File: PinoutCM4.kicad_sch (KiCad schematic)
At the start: 1 part

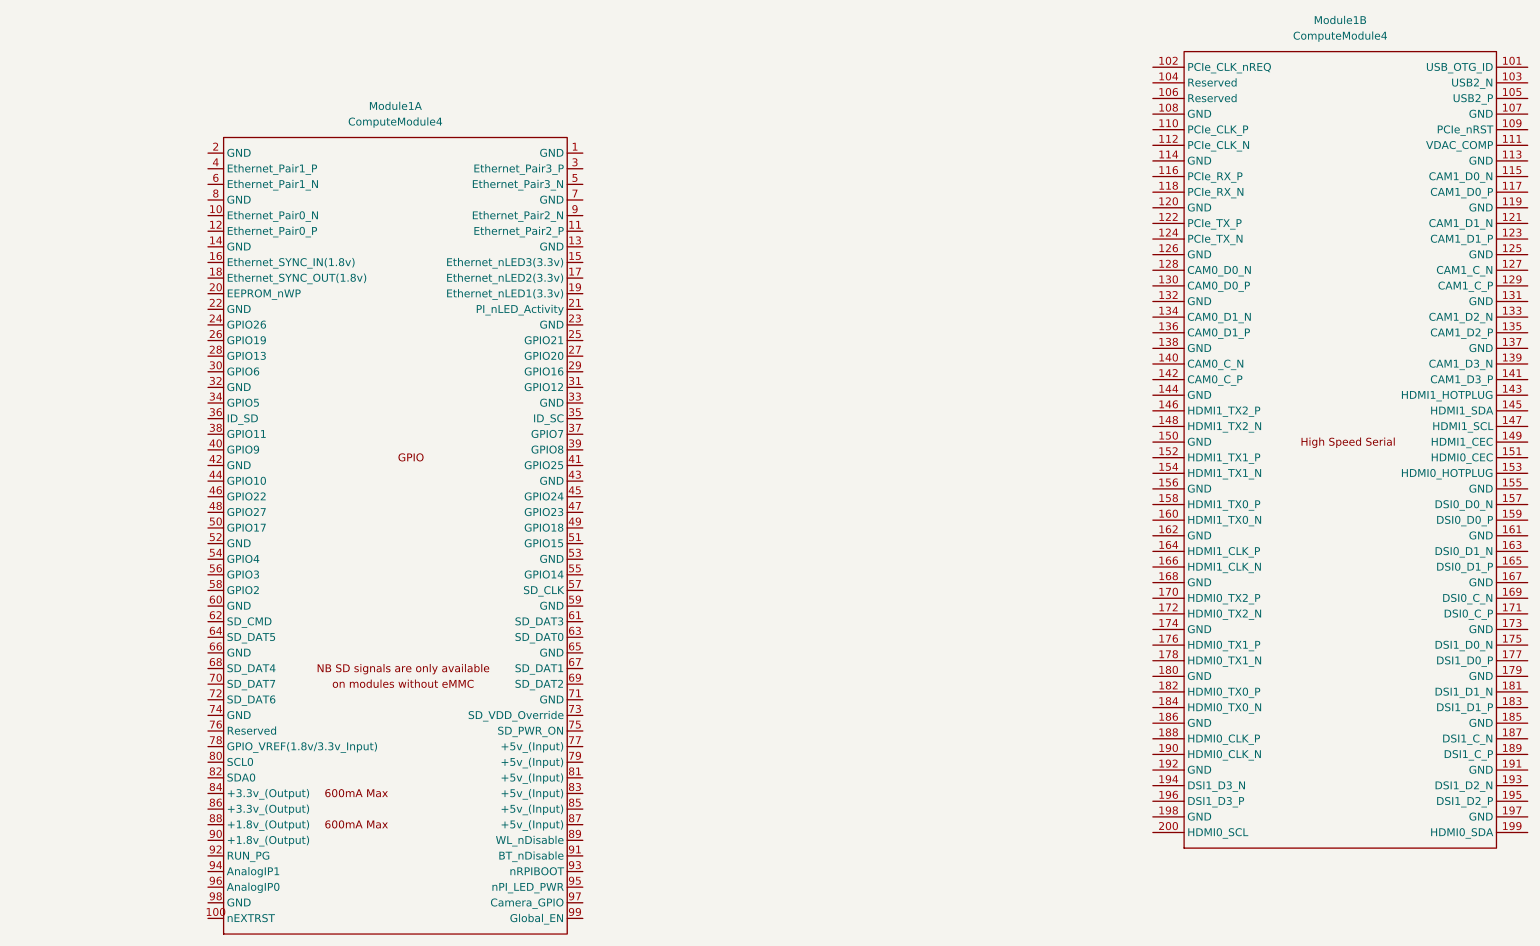
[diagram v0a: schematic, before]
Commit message: Added Indicator LED to CM4
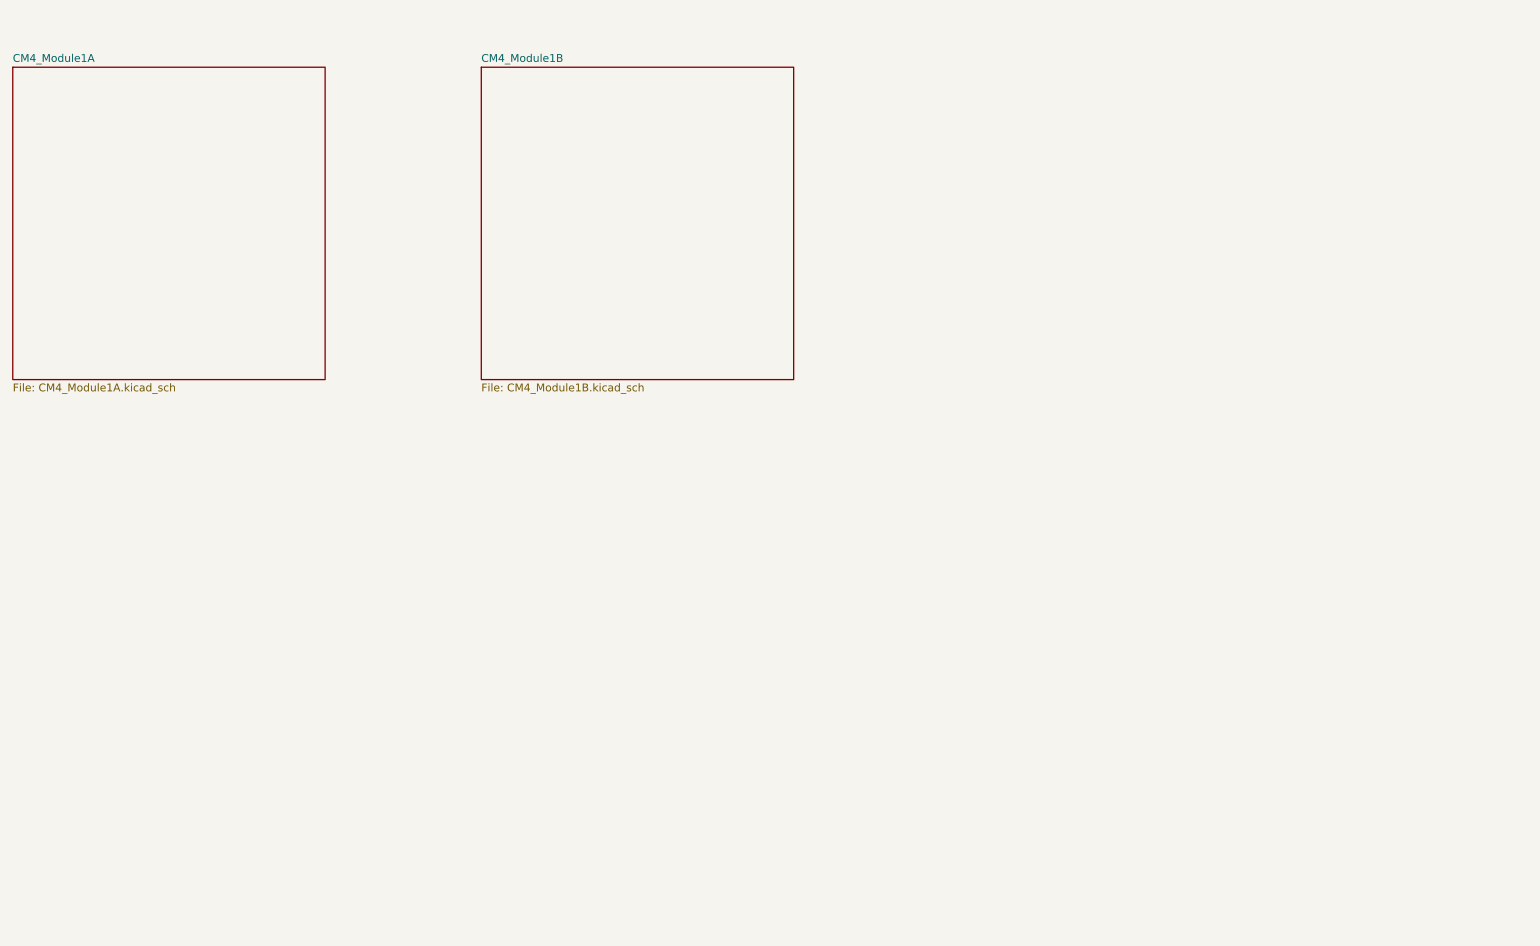
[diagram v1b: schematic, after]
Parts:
- removed Module1: ComputeModule4, CM4IO:Raspberry-Pi-4-Compute-Module, symbol dz_con:DF40C-100DS-0.4V_51_
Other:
- added sheet CM4_Module1A (CM4_Module1A.kicad_sch)
- added sheet CM4_Module1B (CM4_Module1B.kicad_sch)
